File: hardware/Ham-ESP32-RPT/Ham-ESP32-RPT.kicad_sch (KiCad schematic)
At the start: 28 parts, among them J1 5V SUPPLY, J2 12V SUPPLY, J3 RX RADIO, J4 TX RADIO, J5 AUX BTN LED, J6 SPEAKER, Q1 MMBT2222A, SW2 TEST, U1 ESP32-S3-DevKitC-V2, U2 PmodI2S2, U3 INA219AxD

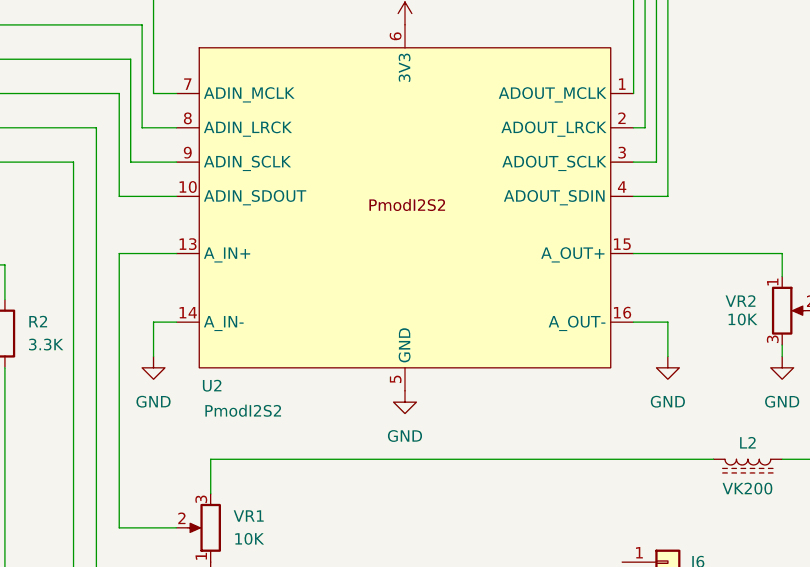
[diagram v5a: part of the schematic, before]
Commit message: Add PmodI2S2 footprint
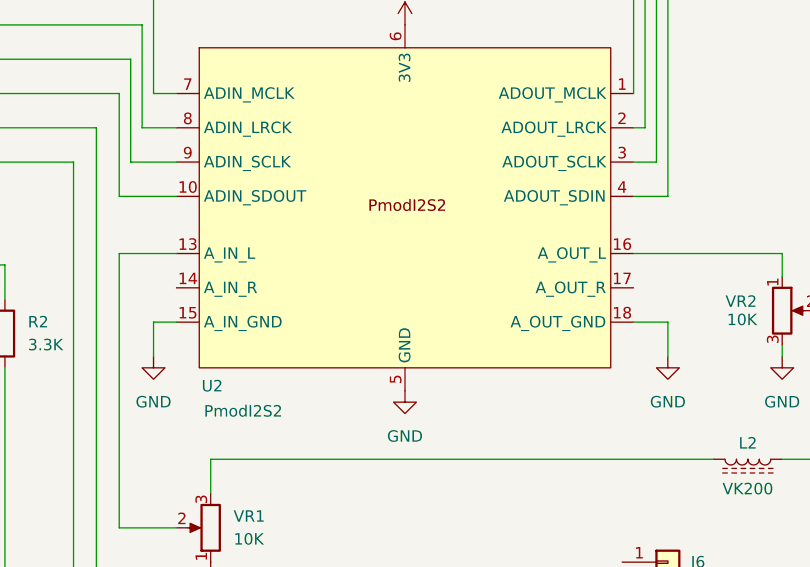
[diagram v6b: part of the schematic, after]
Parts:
- L3: footprint VK200 -> Ham-ESP32-RPT-pretty:VK200
- U2: footprint (none) -> Ham-ESP32-RPT-pretty:PmodI2S2
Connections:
- net GND: now also U2.15 (A_IN_GND), U2.18 (A_OUT_GND); no longer U2.14 (A_IN-), U2.16 (A_OUT-)
- net at VR2.1: now also U2.16 (A_OUT_L); no longer U2.15 (A_OUT+)
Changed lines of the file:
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@@
 			)
 		)
-		(property "Footprint" ""
+		(property "Footprint" "Ham-ESP32-RPT-pretty:PmodI2S2"
 			(at 153.67 90.17 0)
 			(effects
@@
 		)
 		(pin "7"
+		)
+		(pin "18"
+		)
+		(pin "17"
 		)
 		(instances
@@
 			)
 		)
-		(property "Footprint" "VK200"
+		(property "Footprint" "Ham-ESP32-RPT-pretty:VK200"
 			(at 55.88 162.56 0)
 			(effects

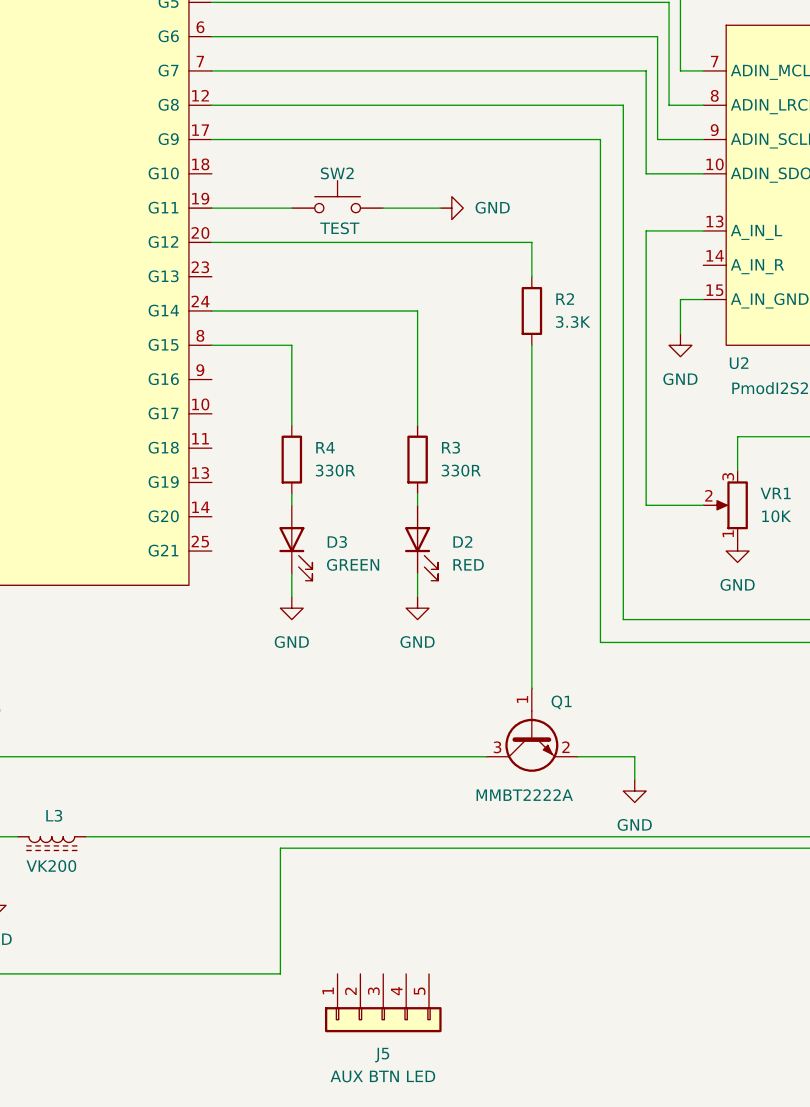
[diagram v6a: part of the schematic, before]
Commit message: Supression pistes
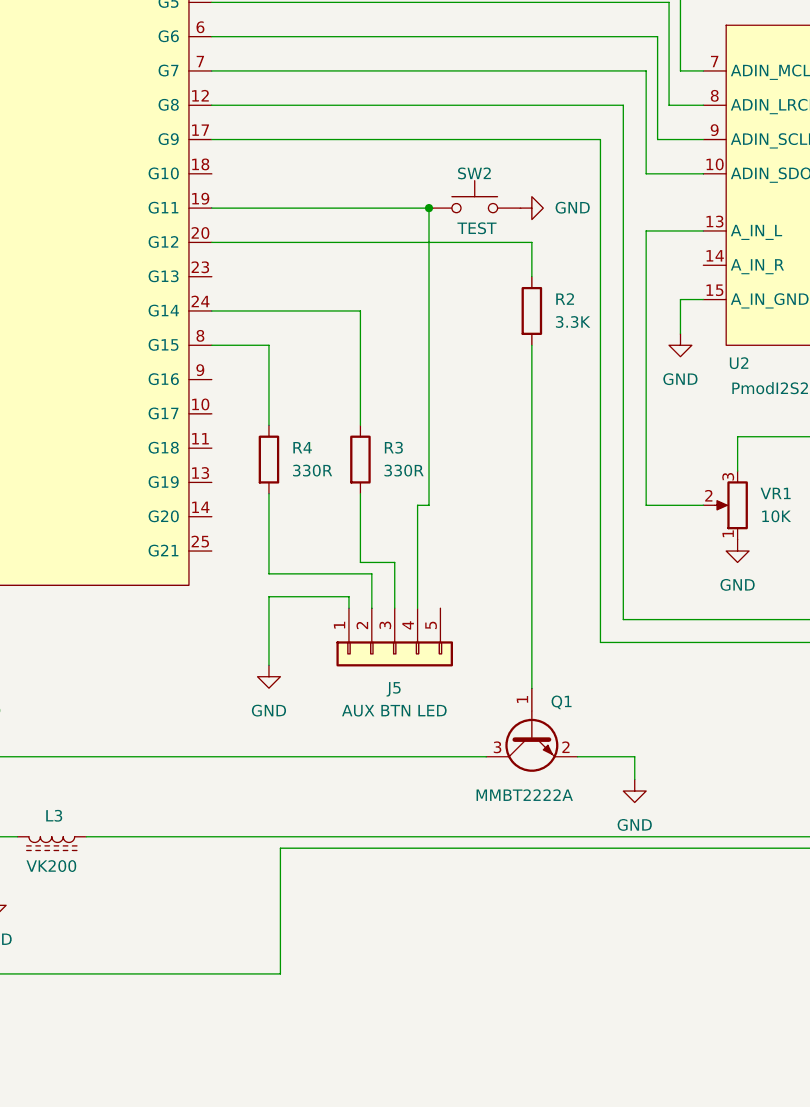
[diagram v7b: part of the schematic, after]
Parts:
- removed D2: RED, LED_SMD:LED_1206_3216Metric, symbol Device:LED
- removed D3: GREEN, LED_SMD:LED_1206_3216Metric, symbol Device:LED
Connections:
- net GND: now also J5.1 (Pin_1)
- net at SW2.1, U1.19 (G11): now also J5.4 (Pin_4)
- net at J5.2 (Pin_2): now also R4.2
- net at J5.3 (Pin_3): now also R3.2
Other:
- moved on the sheet: J5, R3, R4, SW2

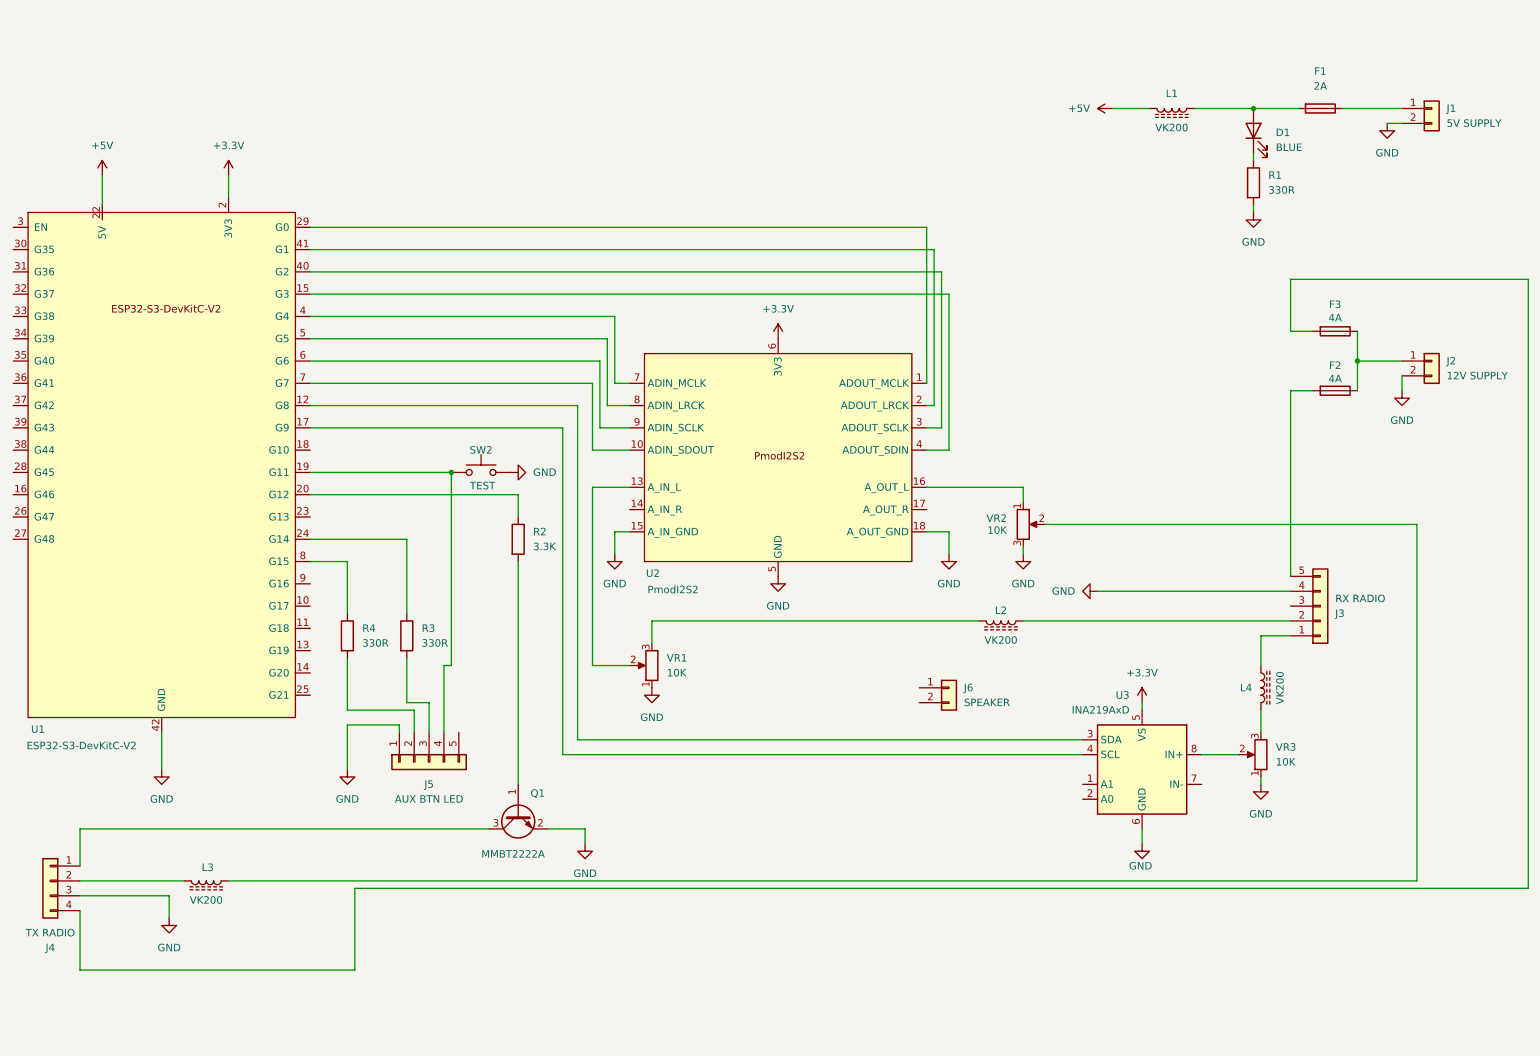
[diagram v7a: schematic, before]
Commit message: update PCB diagram
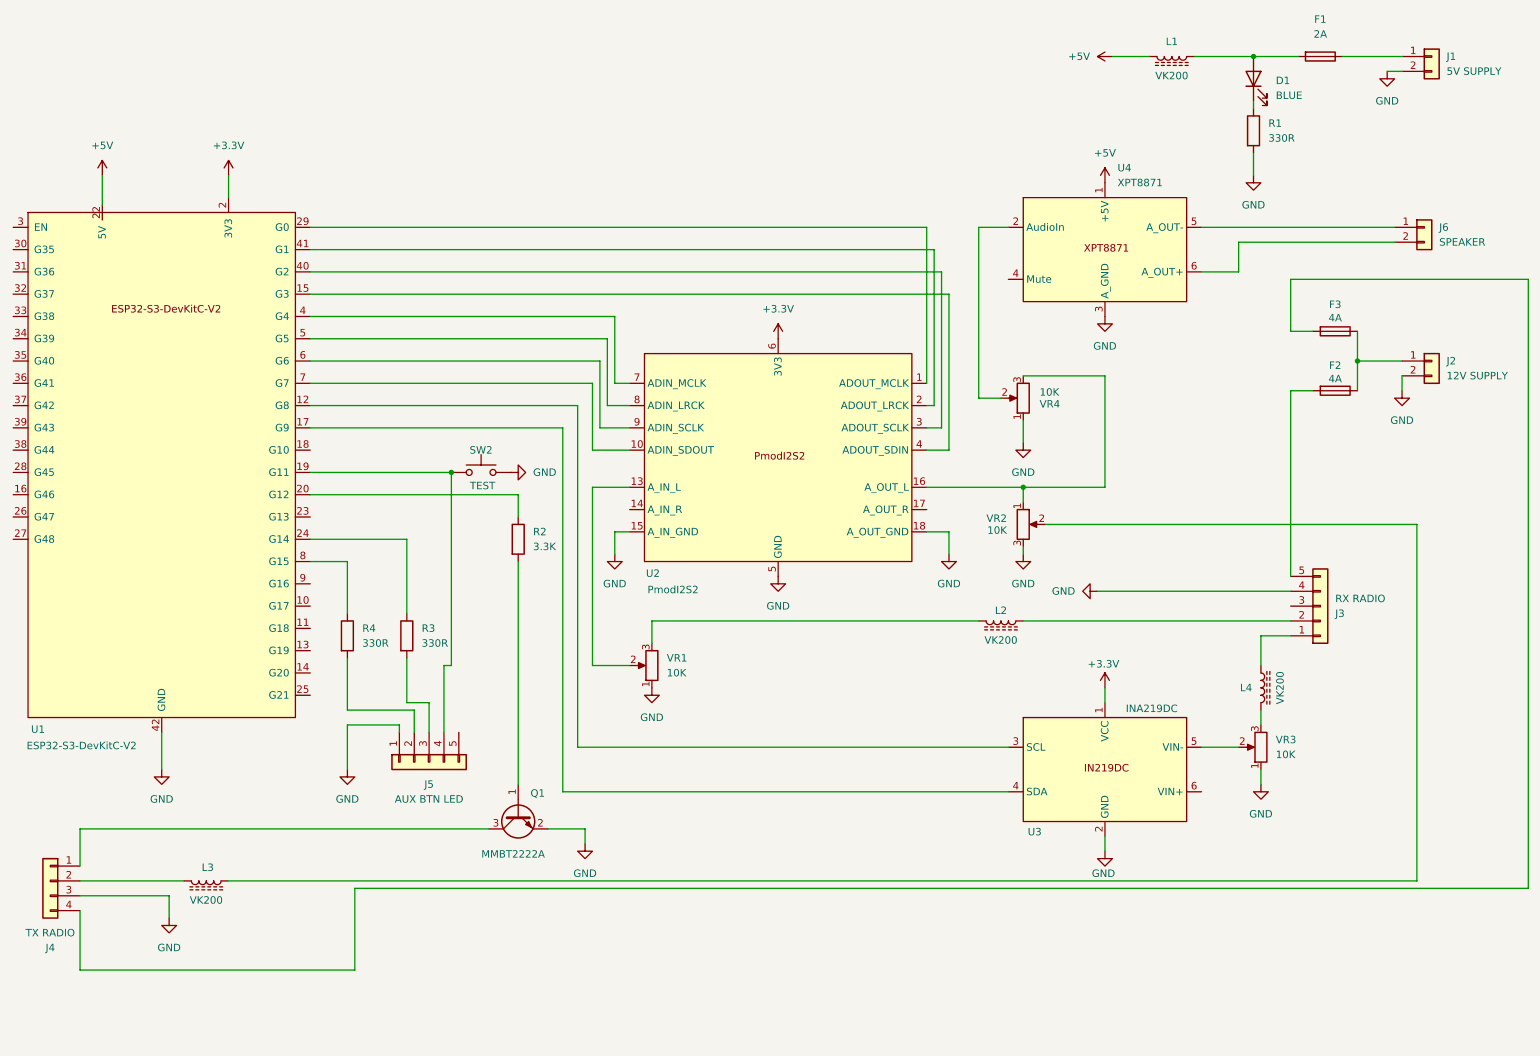
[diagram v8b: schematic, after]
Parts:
- removed U3: INA219AxD, Package_SO:SOIC-8_3.9x4.9mm_P1.27mm, symbol Sensor_Energy:INA219AxD
- added U3: INA219DC, Ham-ESP32-RPT-pretty:INA219DC, symbol Ham-ESP32-RPT:INA219DC
- added U4: XPT8871, Ham-ESP32-RPT-pretty:XPT8871, symbol Ham-ESP32-RPT:XPT8871
- added VR4: 10K, Potentiometer_SMD:Potentiometer_Bourns_3314R-1_Vertical_Hole, symbol Device:R_Potentiometer
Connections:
- net +3.3V: now also U3.1 (VCC), U3.12 (3V3), U4.12 (3V3)
- net +5V: now also U4.1 (+5V)
- net GND: now also U3.11 (GND), U3.2 (GND), U4.3 (A_GND), VR4.1
- net at J6.1 (Pin_1): now also U4.5 (A_OUT-)
- net at J6.2 (Pin_2): now also U4.6 (A_OUT+)
- net at U1.12 (G8): now also U3.3 (SCL)
- net at U1.17 (G9): now also U3.4 (SDA)
- net at U2.16 (A_OUT_L), VR2.1: now also VR4.3
- net at VR3.2: now also U3.5 (VIN-)
- new net: U4.2 (AudioIn), VR4.2
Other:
- moved on the sheet: D1, F1, J1, J6, L1, R1, VR3
